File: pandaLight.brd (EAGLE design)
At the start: 100 x 50 mm, 164 parts, among them J1 PJ-037A, U1 MIC23450AAAYML, U10 51, U11 TPD12S016PWR, U12 N25Q128AF8, U13 TPD12S016PWR, U14 AS4C128M16D3, U15 PMOD-2X6, U16 PMOD-2X6, U17 PLR135-T10, U18 PLT133-T10W, U19 PLR135-T10, U2 6SLX45CSG324, U20 TP10SQ, U21 TP10SQ, U22 PAN1322, U3 TPD4S014SON, U4 FT2232HL, U5 93LC46BT-I/OT, U6 51, U7 51, U8 TPD12S016PWR, U9 51, X1 USBUB-S, X2 HDMI_RECEPTICAL_A, X3 HDMI_RECEPTICAL_A, X4 HDMI_RECEPTICAL_A, Y1 403, Y2 20Mhz

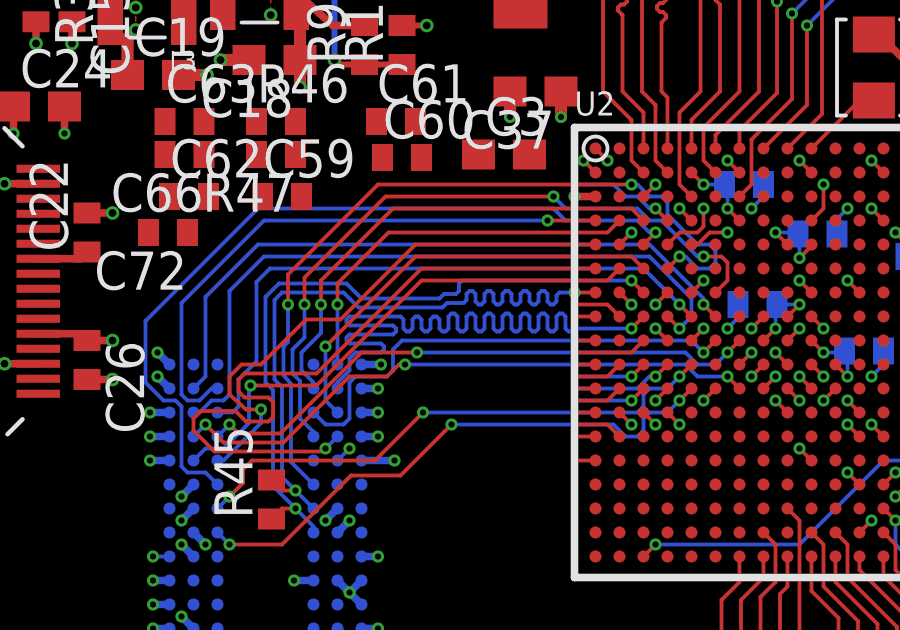
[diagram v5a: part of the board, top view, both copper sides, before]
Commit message: Four signals of the DDR3 address signal group length matched!
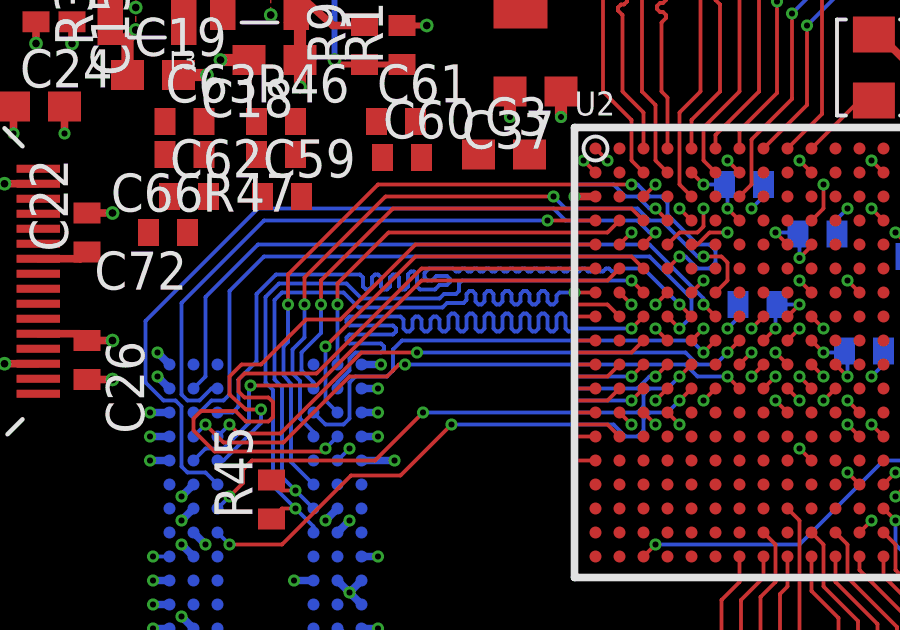
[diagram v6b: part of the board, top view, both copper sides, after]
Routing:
- net DDR3_A2: track 20.5 -> 26.5 mm
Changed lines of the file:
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@@
 <wire x1="34.05" y1="23.2" x2="34.05" y2="24.1" width="0.127" layer="16"/>
 <wire x1="34.05" y1="24.1" x2="34.65" y2="24.7" width="0.127" layer="16"/>
-<wire x1="34.65" y1="24.7" x2="34.65" y2="27.35" width="0.127" layer="16"/>
-<wire x1="34.65" y1="27.35" x2="35.1" y2="27.8" width="0.127" layer="16"/>
-<wire x1="35.1" y1="27.8" x2="47.55" y2="27.8" width="0.127" layer="16"/>
+<wire x1="34.65" y1="24.7" x2="34.65" y2="26.95" width="0.127" layer="16"/>
+<wire x1="34.65" y1="26.95" x2="35.3" y2="27.6" width="0.127" layer="16"/>
+<wire x1="35.3" y1="27.6" x2="38.1" y2="27.6" width="0.127" layer="16"/>
+<wire x1="38.3" y1="27.1" x2="38.4" y2="27.1" width="0.127" layer="16"/>
+<wire x1="38.4" y1="27.1" x2="38.5" y2="27.2" width="0.127" layer="16"/>
+<wire x1="38.5" y1="27.2" x2="38.5" y2="27.5" width="0.127" layer="16"/>
+<wire x1="38.6" y1="27.6" x2="38.7" y2="27.6" width="0.127" layer="16"/>
+<wire x1="38.7" y1="27.6" x2="38.8" y2="27.5" width="0.127" layer="16"/>
+<wire x1="38.8" y1="27.5" x2="38.8" y2="27.2" width="0.127" layer="16"/>
+<wire x1="38.8" y1="27.2" x2="38.9" y2="27.1" width="0.127" layer="16"/>
+<wire x1="38.9" y1="27.1" x2="39" y2="27.1" width="0.127" layer="16"/>
+<wire x1="39" y1="27.1" x2="39.1" y2="27.2" width="0.127" layer="16"/>
+<wire x1="39.1" y1="27.2" x2="39.1" y2="27.5" width="0.127" layer="16"/>
+<wire x1="39.1" y1="27.5" x2="39.2" y2="27.6" width="0.127" layer="16"/>
+<wire x1="39.2" y1="27.6" x2="39.3" y2="27.6" width="0.127" layer="16"/>
+<wire x1="39.3" y1="27.6" x2="39.4" y2="27.5" width="0.127" layer="16"/>
+<wire x1="39.4" y1="27.5" x2="39.4" y2="27.2" width="0.127" layer="16"/>
+<wire x1="39.4" y1="27.2" x2="39.5" y2="27.1" width="0.127" layer="16"/>
+<wire x1="39.5" y1="27.1" x2="39.6" y2="27.1" width="0.127" layer="16"/>
+<wire x1="39.6" y1="27.1" x2="39.7" y2="27.2" width="0.127" layer="16"/>
+<wire x1="39.7" y1="27.2" x2="39.7" y2="27.6" width="0.127" layer="16"/>
+<wire x1="39.7" y1="27.6" x2="39.8" y2="27.7" width="0.127" layer="16"/>
+<wire x1="39.8" y1="27.7" x2="39.9" y2="27.7" width="0.127" layer="16"/>
+<wire x1="39.9" y1="27.7" x2="40" y2="27.6" width="0.127" layer="16"/>
+<wire x1="40" y1="27.6" x2="40" y2="27.2" width="0.127" layer="16"/>
+<wire x1="40" y1="27.2" x2="40.1" y2="27.1" width="0.127" layer="16"/>
+<wire x1="40.4" y1="27.8" x2="41.2" y2="27.8" width="0.127" layer="16"/>
+<wire x1="41.2" y1="27.8" x2="41.3" y2="27.7" width="0.127" layer="16"/>
+<wire x1="41.3" y1="27.7" x2="41.4" y2="27.7" width="0.127" layer="16"/>
+<wire x1="41.4" y1="27.7" x2="41.5" y2="27.8" width="0.127" layer="16"/>
+<wire x1="41.5" y1="27.8" x2="41.6" y2="27.8" width="0.127" layer="16"/>
+<wire x1="41.6" y1="27.8" x2="41.7" y2="27.7" width="0.127" layer="16"/>
+<wire x1="41.7" y1="27.7" x2="41.8" y2="27.7" width="0.127" layer="16"/>
+<wire x1="41.8" y1="27.7" x2="41.9" y2="27.8" width="0.127" layer="16"/>
+<wire x1="41.9" y1="27.8" x2="42" y2="27.8" width="0.127" layer="16"/>
+<wire x1="42" y1="27.8" x2="42.1" y2="27.7" width="0.127" layer="16"/>
+<wire x1="42.1" y1="27.7" x2="42.2" y2="27.7" width="0.127" layer="16"/>
+<wire x1="42.2" y1="27.7" x2="42.3" y2="27.8" width="0.127" layer="16"/>
+<wire x1="42.3" y1="27.8" x2="42.4" y2="27.8" width="0.127" layer="16"/>
+<wire x1="42.4" y1="27.8" x2="42.5" y2="27.7" width="0.127" layer="16"/>
+<wire x1="42.5" y1="27.7" x2="42.6" y2="27.7" width="0.127" layer="16"/>
+<wire x1="42.6" y1="27.7" x2="42.7" y2="27.8" width="0.127" layer="16"/>
+<wire x1="42.7" y1="27.8" x2="42.8" y2="27.8" width="0.127" layer="16"/>
+<wire x1="42.8" y1="27.8" x2="42.9" y2="27.7" width="0.127" layer="16"/>
+<wire x1="42.9" y1="27.7" x2="43" y2="27.7" width="0.127" layer="16"/>
+<wire x1="43" y1="27.7" x2="43.1" y2="27.8" width="0.127" layer="16"/>
+<wire x1="43.1" y1="27.8" x2="43.2" y2="27.8" width="0.127" layer="16"/>
+<wire x1="43.2" y1="27.8" x2="43.3" y2="27.7" width="0.127" layer="16"/>
+<wire x1="43.3" y1="27.7" x2="43.4" y2="27.7" width="0.127" layer="16"/>
+<wire x1="43.4" y1="27.7" x2="43.5" y2="27.8" width="0.127" layer="16"/>
+<wire x1="43.5" y1="27.8" x2="43.6" y2="27.8" width="0.127" layer="16"/>
+<wire x1="43.6" y1="27.8" x2="43.7" y2="27.7" width="0.127" layer="16"/>
+<wire x1="43.7" y1="27.7" x2="43.8" y2="27.7" width="0.127" layer="16"/>
+<wire x1="43.8" y1="27.7" x2="43.9" y2="27.8" width="0.127" layer="16"/>
+<wire x1="43.9" y1="27.8" x2="44" y2="27.8" width="0.127" layer="16"/>
+<wire x1="44" y1="27.8" x2="44.1" y2="27.7" width="0.127" layer="16"/>
+<wire x1="44.1" y1="27.7" x2="44.2" y2="27.7" width="0.127" layer="16"/>
+<wire x1="44.2" y1="27.7" x2="44.3" y2="27.8" width="0.127" layer="16"/>
+<wire x1="44.3" y1="27.8" x2="44.4" y2="27.8" width="0.127" layer="16"/>
+<wire x1="44.4" y1="27.8" x2="44.5" y2="27.7" width="0.127" layer="16"/>
+<wire x1="44.5" y1="27.7" x2="44.6" y2="27.7" width="0.127" layer="16"/>
+<wire x1="44.6" y1="27.7" x2="44.7" y2="27.8" width="0.127" layer="16"/>
+<wire x1="44.7" y1="27.8" x2="44.8" y2="27.8" width="0.127" layer="16"/>
+<wire x1="44.8" y1="27.8" x2="44.9" y2="27.7" width="0.127" layer="16"/>
+<wire x1="44.9" y1="27.7" x2="45" y2="27.7" width="0.127" layer="16"/>
+<wire x1="45" y1="27.7" x2="45.1" y2="27.8" width="0.127" layer="16"/>
+<wire x1="45.1" y1="27.8" x2="45.2" y2="27.8" width="0.127" layer="16"/>
+<wire x1="45.2" y1="27.8" x2="45.3" y2="27.7" width="0.127" layer="16"/>
+<wire x1="45.3" y1="27.7" x2="45.4" y2="27.7" width="0.127" layer="16"/>
+<wire x1="45.4" y1="27.7" x2="45.5" y2="27.8" width="0.127" layer="16"/>
+<wire x1="45.5" y1="27.8" x2="45.6" y2="27.8" width="0.127" layer="16"/>
+<wire x1="45.6" y1="27.8" x2="45.7" y2="27.7" width="0.127" layer="16"/>
+<wire x1="45.7" y1="27.7" x2="45.8" y2="27.7" width="0.127" layer="16"/>
+<wire x1="45.8" y1="27.7" x2="45.9" y2="27.8" width="0.127" layer="16"/>
+<wire x1="45.9" y1="27.8" x2="46" y2="27.8" width="0.127" layer="16"/>
+<wire x1="46" y1="27.8" x2="46.1" y2="27.7" width="0.127" layer="16"/>
+<wire x1="46.1" y1="27.7" x2="46.2" y2="27.7" width="0.127" layer="16"/>
+<wire x1="46.2" y1="27.7" x2="46.3" y2="27.8" width="0.127" layer="16"/>
+<wire x1="46.3" y1="27.8" x2="46.4" y2="27.8" width="0.127" layer="16"/>
+<wire x1="46.4" y1="27.8" x2="46.5" y2="27.7" width="0.127" layer="16"/>
+<wire x1="46.5" y1="27.7" x2="46.6" y2="27.7" width="0.127" layer="16"/>
+<wire x1="46.6" y1="27.7" x2="46.7" y2="27.8" width="0.127" layer="16"/>
+<wire x1="46.7" y1="27.8" x2="47.55" y2="27.8" width="0.127" layer="16"/>
 <via x="48.75" y="26.6" extent="1-16" drill="0.2032"/>
 <wire x1="48.75" y1="26.6" x2="49.15" y2="26.2" width="0.127" layer="1"/>
 <wire x1="47.55" y1="27.8" x2="48.75" y2="26.6" width="0.127" layer="16"/>
+<wire x1="40.1" y1="27.1" x2="40.6" y2="27.1" width="0.127" layer="16"/>
+<wire x1="40.6" y1="27.1" x2="40.75" y2="27.25" width="0.127" layer="16"/>
+<wire x1="40.75" y1="27.25" x2="41" y2="27.25" width="0.127" layer="16"/>
+<wire x1="41" y1="27.25" x2="41.1" y2="27.35" width="0.127" layer="16"/>
+<wire x1="41.1" y1="27.35" x2="41.1" y2="27.45" width="0.127" layer="16"/>
+<wire x1="41.1" y1="27.45" x2="41" y2="27.55" width="0.127" layer="16"/>
+<wire x1="41" y1="27.55" x2="40.65" y2="27.55" width="0.127" layer="16"/>
+<wire x1="40.65" y1="27.55" x2="40.5" y2="27.4" width="0.127" layer="16"/>
+<wire x1="40.5" y1="27.4" x2="40.35" y2="27.4" width="0.127" layer="16"/>
+<wire x1="40.35" y1="27.4" x2="40.25" y2="27.5" width="0.127" layer="16"/>
+<wire x1="40.25" y1="27.5" x2="40.25" y2="27.65" width="0.127" layer="16"/>
+<wire x1="40.25" y1="27.65" x2="40.4" y2="27.8" width="0.127" layer="16"/>
+<wire x1="38.5" y1="27.5" x2="38.6" y2="27.6" width="0.127" layer="16"/>
+<wire x1="38.1" y1="27.6" x2="38.2" y2="27.5" width="0.127" layer="16"/>
+<wire x1="38.2" y1="27.5" x2="38.2" y2="27.2" width="0.127" layer="16"/>
+<wire x1="38.2" y1="27.2" x2="38.3" y2="27.1" width="0.127" layer="16"/>
 </signal>
 <signal name="DDR3_A3">

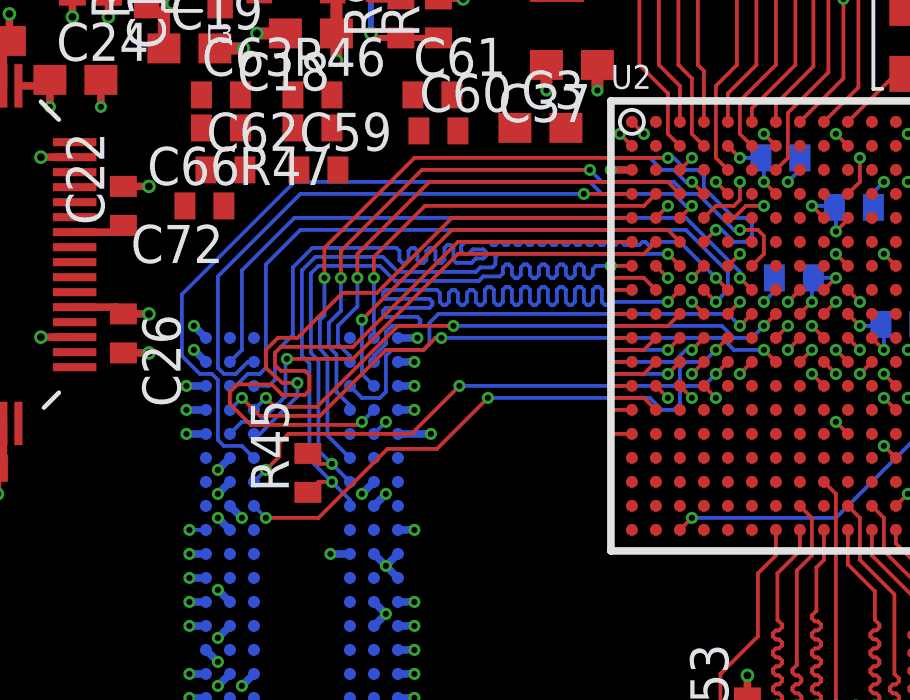
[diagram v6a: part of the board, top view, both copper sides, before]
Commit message: Length matched a whole lot of signals!
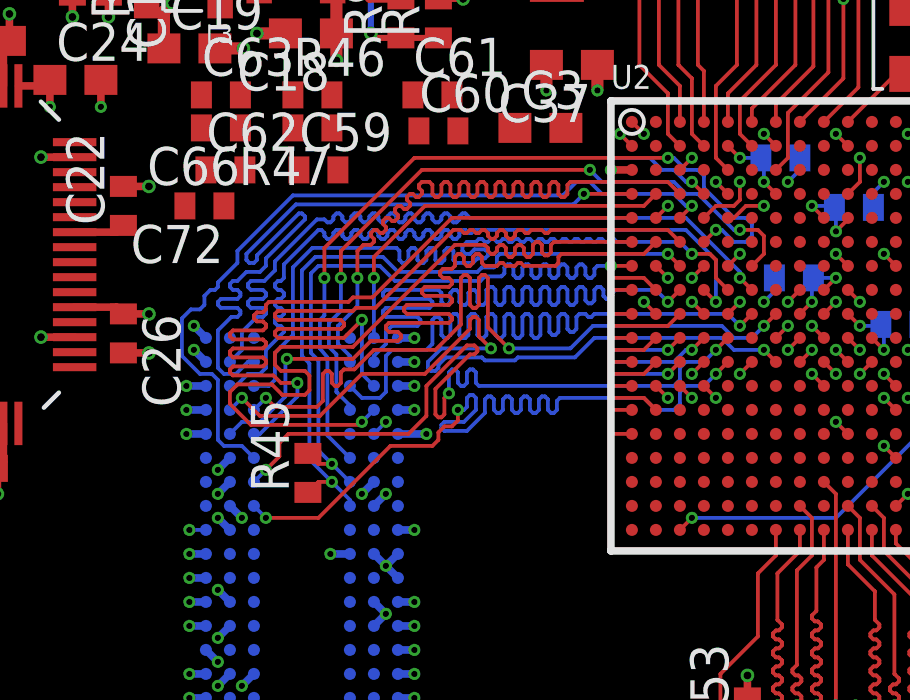
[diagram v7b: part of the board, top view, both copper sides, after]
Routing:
- net DDR3_A4: track 14.4 -> 26.5 mm
- net DDR3_A1: track 16.2 -> 26.5 mm
- net DDR3_BA0: track 17.6 -> 26.5 mm
- net DDR3_CAS#: track 18.3 -> 26.5 mm
- net DDR3_BA2: track 18.3 -> 26.4 mm
- net DDR3_A11: track 15.9 -> 24.0 mm
- net DDR3_RAS#: track 18.7 -> 26.5 mm
- net DDR3_A0: track 19.3 -> 26.5 mm
- net DDR3_A9: track 19.4 -> 26.5 mm
- net DDR3_A3: track 20.0 -> 26.5 mm
- net DDR3_A7: track 22.1 -> 26.5 mm
- net DDR3_A5: track 23.1 -> 26.5 mm
- net DDR3_BA1: track 24.3 -> 26.5 mm
- net +1V5: track 33.6 -> 34.1 mm, vias 29 -> 30

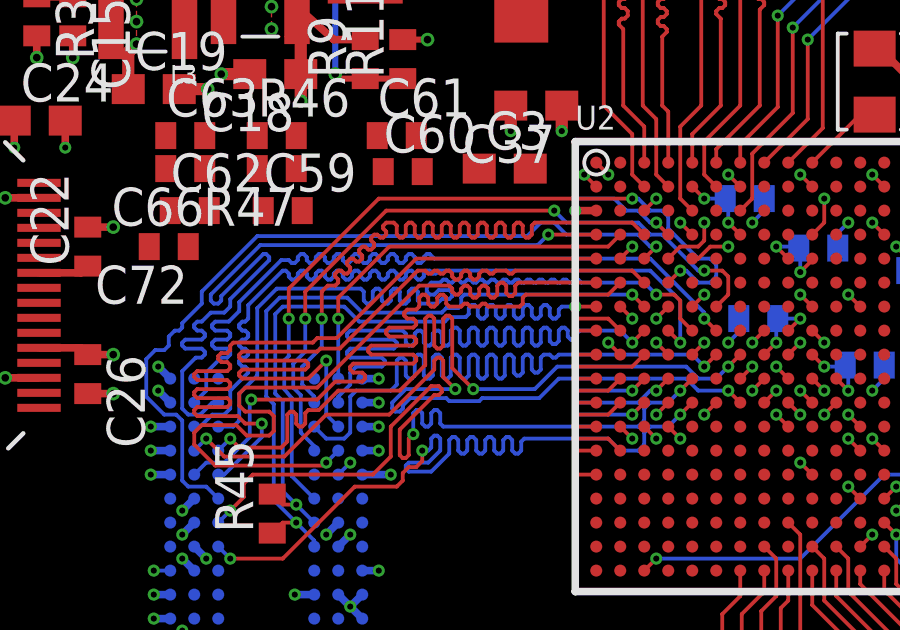
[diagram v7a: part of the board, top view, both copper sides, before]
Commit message: Finished length matching the DDR3 address trace group!
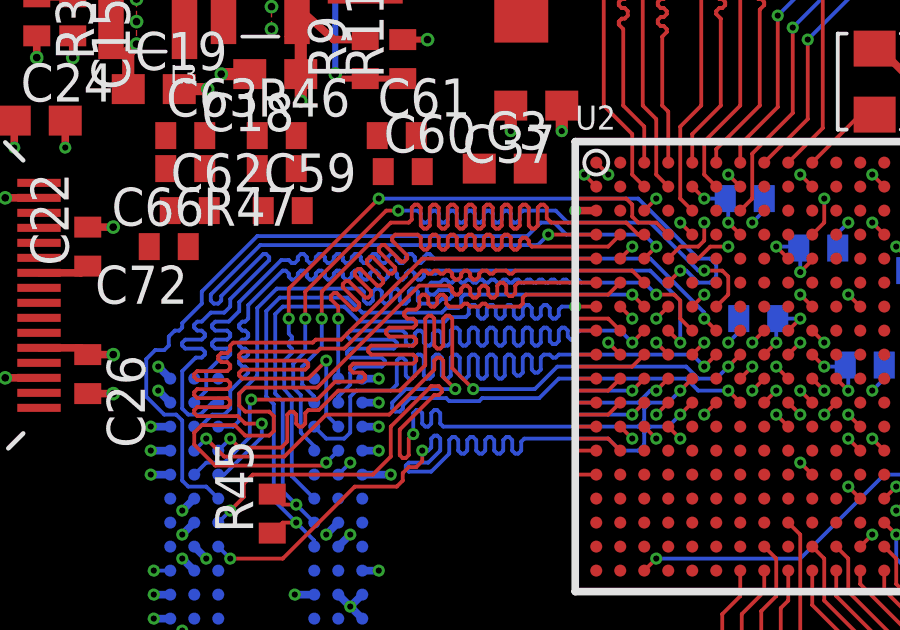
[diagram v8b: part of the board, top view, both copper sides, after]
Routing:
- net DDR3_A8: track 13.0 -> 26.5 mm
- net DDR3_A12: track 23.1 -> 26.4 mm
- net DDR3_A11: track 24.0 -> 26.5 mm
- net N$35: track 3.60 -> 3.83 mm, vias 1 -> 0
